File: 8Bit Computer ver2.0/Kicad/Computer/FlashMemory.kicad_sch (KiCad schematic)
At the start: 0 parts

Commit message: Kicad,parts
Kicad:
worked on Flash memory
began RAM
parts:
added Delay Chip for Flash
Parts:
- added IC189: SN74AHC74DR, Samacsys:SOIC127P600X175-14N, symbol Samacsys:SN74AHC74DR
- added IC190, IC192: M29F800FT55N3E2, Samacsys:SOP50P2000X120-48N, symbol Samacsys:M29F800FT55N3E2
- added IC193, IC194, IC195, IC196, IC197, IC198, IC199, IC200, IC201, IC202, IC203, IC204, IC205, IC206: SN74ABT245BDWR, Samacsys:SOIC127P1030X265-20N, symbol Samacsys:SN74ABT245BDWR
- added J1, J2: Conn_02x25_Odd_Even, Connector_PinHeader_2.54mm:PinHeader_2x25_P2.54mm_Vertical, symbol Connector_Generic:Conn_02x25_Odd_Even
- added R1, R10, R2, R3, R4, R5, R6, R7, R8, R9: 4.7k, Resistor_SMD:R_1206_3216Metric_Pad1.30x1.75mm_HandSolder, symbol Device:R
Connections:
- net ADR_{dis}: now also IC189.12 (2D)
- net DAT_{dis}: now also IC189.2 (1D)
- new net: IC204.11 (B8), IC206.9 (A8)
- new net: IC204.12 (B7), IC206.8 (A7)
- new net: IC204.13 (B6), IC206.7 (A6)
- new net: IC204.14 (B5), IC206.6 (A5)
- new net: IC204.15 (B4), IC206.5 (A4)
- new net: IC204.16 (B3), IC206.4 (A3)
- new net: IC204.17 (B2), IC206.3 (A2)
- new net: IC204.18 (B1), IC206.2 (A1)
- new net: IC189.8 (2~{Q}), IC205.19 (~{OE}), IC206.19 (~{OE})
- new net: IC203.18 (B1), IC205.2 (A1)
- new net: IC203.17 (B2), IC205.3 (A2)
- new net: IC203.16 (B3), IC205.4 (A3)
- new net: IC203.15 (B4), IC205.5 (A4)
- new net: IC203.14 (B5), IC205.6 (A5)
- new net: IC203.13 (B6), IC205.7 (A6)
- new net: IC203.12 (B7), IC205.8 (A7)
- new net: IC203.11 (B8), IC205.9 (A8)
- new net: IC189.6 (1~{Q}), IC198.19 (~{OE})
- new net ADR0: IC206.11 (B8)
- new net ADR1: IC206.13 (B6)
- new net ADR10: IC206.16 (B3)
- new net ADR11: IC206.18 (B1)
- new net ADR12: IC205.12 (B7)
- new net ADR13: IC205.14 (B5)
- new net ADR14: IC205.16 (B3)
- new net ADR15: IC205.18 (B1)
- new net ADR2: IC206.15 (B4)
- new net ADR3: IC206.17 (B2)
- new net ADR4: IC205.11 (B8)
- new net ADR5: IC205.13 (B6)
- new net ADR6: IC205.15 (B4)
- new net ADR7: IC205.17 (B2)
- new net ADR8: IC206.12 (B7)
- new net ADR9: IC206.14 (B5)
- new net AMISC0: IC192.11 (WE#), IC197.18 (B1), J1.21 (Pin_21)
- new net AMISC1: IC192.12 (RP#), J1.23 (Pin_23)
- new net AMISC2: IC192.15 (R/B#), J1.29 (Pin_29)
- new net AMISC3: IC192.16 (A18), IC197.15 (B4), J1.31 (Pin_31)
- new net AMISC4: IC192.17 (A17), IC197.14 (B5), J1.33 (Pin_33)
- new net BMISC0: IC192.48 (A16), IC197.13 (B6), J1.2 (Pin_2)
- new net BMISC1: IC192.28 (OE#), IC197.12 (B7), J1.42 (Pin_42)
- new net BMISC2: IC192.26 (CE#), IC197.11 (B8), J1.46 (Pin_46)
- new net CMD0: IC199.11 (B8)
- new net CMD1: IC199.12 (B7)
- new net CMD2: IC199.13 (B6)
- new net CMD3: IC199.14 (B5)
- new net CMD4: IC199.15 (B4)
- new net CMD5: IC199.16 (B3)
- new net CMD6: IC199.17 (B2)
- new net CMD7: IC199.18 (B1)
- new net CMISC0: IC190.11 (WE#), IC202.18 (B1), J2.21 (Pin_21)
- new net CMISC1: IC190.12 (RP#), J2.23 (Pin_23)
- new net CMISC2: IC190.15 (R/B#), J2.29 (Pin_29)
- new net CMISC3: IC190.16 (A18), IC202.15 (B4), J2.31 (Pin_31)
- new net CMISC4: IC190.17 (A17), IC202.14 (B5), J2.33 (Pin_33)
- new net DAT0: IC198.11 (B8)
- new net DAT1: IC198.12 (B7)
- new net DAT2: IC198.13 (B6)
- new net DAT3: IC198.14 (B5)
- new net DAT4: IC198.15 (B4)
- new net DAT5: IC198.16 (B3)
- new net DAT6: IC198.17 (B2)
- new net DAT7: IC198.18 (B1)
- new net DATCMD0: IC192.45 (DQ15A-1), IC195.2 (A1), J1.8 (Pin_8)
- new net DATCMD1: IC192.44 (DQ7), IC195.3 (A2), J1.10 (Pin_10)
- new net DATCMD10: IC192.34 (DQ10), IC196.4 (A3), J1.30 (Pin_30)
- new net DATCMD11: IC192.33 (DQ2), IC196.5 (A4), J1.32 (Pin_32)
- new net DATCMD12: IC192.32 (DQ9), IC196.6 (A5), J1.34 (Pin_34)
- new net DATCMD13: IC192.31 (DQ1), IC196.7 (A6), J1.36 (Pin_36)
- new net DATCMD14: IC192.30 (DQ8), IC196.8 (A7), J1.38 (Pin_38)
- new net DATCMD15: IC192.29 (DQ0), IC196.9 (A8), J1.40 (Pin_40)
- new net DATCMD2: IC192.43 (DQ14), IC195.4 (A3), J1.12 (Pin_12)
- new net DATCMD3: IC192.42 (DQ6), IC195.5 (A4), J1.14 (Pin_14)
- new net DATCMD4: IC192.41 (DQ13), IC195.6 (A5), J1.16 (Pin_16)
- new net DATCMD5: IC192.40 (DQ5), IC195.7 (A6), J1.18 (Pin_18)
- new net DATCMD6: IC192.39 (DQ12), IC195.8 (A7), J1.20 (Pin_20)
- new net DATCMD7: IC192.38 (DQ4), IC195.9 (A8), J1.22 (Pin_22)
- new net DATCMD8: IC192.36 (DQ11), IC196.2 (A1), J1.26 (Pin_26)
- new net DATCMD9: IC192.35 (DQ3), IC196.3 (A2), J1.28 (Pin_28)
- new net DMISC0: IC190.48 (A16), IC202.13 (B6), J2.2 (Pin_2)
- new net DMISC1: IC190.28 (OE#), IC202.12 (B7), J2.42 (Pin_42)
- new net DMISC2: IC190.26 (CE#), IC202.11 (B8), J2.46 (Pin_46)
- new net GND: IC189.7 (GND), IC190.27 (VSS_1), IC190.46 (VSS_2), IC192.27 (VSS_1), IC192.46 (VSS_2), IC193.10 (GND), IC194.10 (GND), IC195.10 (GND), IC196.10 (GND), IC197.10 (GND), IC197.5 (A4), IC197.6 (A5), IC197.7 (A6), IC197.8 (A7), IC197.9 (A8), IC198.10 (GND), IC199.10 (GND), IC199.19 (~{OE}), IC200.10 (GND), IC201.10 (GND), IC202.10 (GND), IC202.5 (A4), IC202.6 (A5), IC202.7 (A6), IC202.8 (A7), IC202.9 (A8), IC203.10 (GND), IC204.10 (GND), IC205.10 (GND), IC206.10 (GND), J1.44 (Pin_44), J1.6 (Pin_6), J2.44 (Pin_44), J2.6 (Pin_6), R1.1, R10.1, R2.1, R3.1, R4.1, R5.1, R6.1, R7.1, R8.1, R9.1
- new net HADR0: IC190.45 (DQ15A-1), IC203.2 (A1), J2.8 (Pin_8)
- new net HADR1: IC190.44 (DQ7), IC203.3 (A2), J2.10 (Pin_10)
- new net HADR10: IC190.34 (DQ10), IC204.4 (A3), J2.30 (Pin_30)
- new net HADR11: IC190.33 (DQ2), IC204.5 (A4), J2.32 (Pin_32)
- new net HADR12: IC190.32 (DQ9), IC204.6 (A5), J2.34 (Pin_34)
- new net HADR13: IC190.31 (DQ1), IC204.7 (A6), J2.36 (Pin_36)
- new net HADR14: IC190.30 (DQ8), IC204.8 (A7), J2.38 (Pin_38)
- new net HADR15: IC190.29 (DQ0), IC204.9 (A8), J2.40 (Pin_40)
- new net HADR2: IC190.43 (DQ14), IC203.4 (A3), J2.12 (Pin_12)
- new net HADR3: IC190.42 (DQ6), IC203.5 (A4), J2.14 (Pin_14)
- new net HADR4: IC190.41 (DQ13), IC203.6 (A5), J2.16 (Pin_16)
- new net HADR5: IC190.40 (DQ5), IC203.7 (A6), J2.18 (Pin_18)
- new net HADR6: IC190.39 (DQ12), IC203.8 (A7), J2.20 (Pin_20)
- new net HADR7: IC190.38 (DQ4), IC203.9 (A8), J2.22 (Pin_22)
- new net HADR8: IC190.36 (DQ11), IC204.2 (A1), J2.26 (Pin_26)
- new net HADR9: IC190.35 (DQ3), IC204.3 (A2), J2.28 (Pin_28)
- new net HDATCMD0: IC195.18 (B1), IC198.2 (A1)
- new net HDATCMD1: IC195.17 (B2), IC199.2 (A1)
- new net HDATCMD10: IC196.16 (B3), IC198.7 (A6)
- new net HDATCMD11: IC196.15 (B4), IC199.7 (A6)
- new net HDATCMD12: IC196.14 (B5), IC198.8 (A7)
- new net HDATCMD13: IC196.13 (B6), IC199.8 (A7)
- new net HDATCMD14: IC196.12 (B7), IC198.9 (A8)
- new net HDATCMD15: IC196.11 (B8), IC199.9 (A8)
- new net HDATCMD2: IC195.16 (B3), IC198.3 (A2)
- new net HDATCMD3: IC195.15 (B4), IC199.3 (A2)
- new net HDATCMD4: IC195.14 (B5), IC198.4 (A3)
- new net HDATCMD5: IC195.13 (B6), IC199.4 (A3)
- new net HDATCMD6: IC195.12 (B7), IC198.5 (A4)
- new net HDATCMD7: IC195.11 (B8), IC199.5 (A4)
- new net HDATCMD8: IC196.18 (B1), IC198.6 (A5)
- new net HDATCMD9: IC196.17 (B2), IC199.6 (A5)
- new net LN0: IC194.9 (A8), IC201.9 (A8)
- new net LN1: IC194.8 (A7), IC201.8 (A7)
- new net LN10: IC193.7 (A6), IC200.7 (A6)
- new net LN11: IC193.6 (A5), IC200.6 (A5)
- new net LN12: IC193.5 (A4), IC200.5 (A4)
- new net LN13: IC193.4 (A3), IC200.4 (A3)
- new net LN14: IC193.3 (A2), IC200.3 (A2)
- new net LN15: IC193.2 (A1), IC200.2 (A1)
- new net LN2: IC194.7 (A6), IC201.7 (A6)
- new net LN3: IC194.6 (A5), IC201.6 (A5)
- new net LN4: IC194.5 (A4), IC201.5 (A4)
- new net LN5: IC194.4 (A3), IC201.4 (A3)
- new net LN6: IC194.3 (A2), IC201.3 (A2)
- new net LN7: IC194.2 (A1), IC201.2 (A1)
- new net LN8: IC193.9 (A8), IC200.9 (A8)
- new net LN9: IC193.8 (A7), IC200.8 (A7)
- new net LNHADR0: IC190.1 (A15), IC200.18 (B1), J2.1 (Pin_1)
- new net LNHADR1: IC190.2 (A14), IC200.17 (B2), J2.3 (Pin_3)
- new net LNHADR10: IC190.20 (A5), IC201.16 (B3), J2.39 (Pin_39)
- new net LNHADR11: IC190.21 (A4), IC201.15 (B4), J2.41 (Pin_41)
- new net LNHADR12: IC190.22 (A3), IC201.14 (B5), J2.43 (Pin_43)
- new net LNHADR13: IC190.23 (A2), IC201.13 (B6), J2.45 (Pin_45)
- new net LNHADR14: IC190.24 (A1), IC201.12 (B7), J2.47 (Pin_47)
- new net LNHADR15: IC190.25 (A0), IC201.11 (B8), J2.48 (Pin_48)
- new net LNHADR2: IC190.3 (A13), IC200.16 (B3), J2.5 (Pin_5)
- new net LNHADR3: IC190.4 (A12), IC200.15 (B4), J2.7 (Pin_7)
- new net LNHADR4: IC190.5 (A11), IC200.14 (B5), J2.9 (Pin_9)
- new net LNHADR5: IC190.6 (A10), IC200.13 (B6), J2.11 (Pin_11)
- new net LNHADR6: IC190.7 (A9), IC200.12 (B7), J2.13 (Pin_13)
- new net LNHADR7: IC190.8 (A8), IC200.11 (B8), J2.15 (Pin_15)
- new net LNHADR8: IC190.18 (A7), IC201.18 (B1), J2.35 (Pin_35)
- new net LNHADR9: IC190.19 (A6), IC201.17 (B2), J2.37 (Pin_37)
- new net LNHCD0: IC192.1 (A15), IC193.18 (B1), J1.1 (Pin_1)
- new net LNHCD1: IC192.2 (A14), IC193.17 (B2), J1.3 (Pin_3)
- new net LNHCD10: IC192.20 (A5), IC194.16 (B3), J1.39 (Pin_39)
- new net LNHCD11: IC192.21 (A4), IC194.15 (B4), J1.41 (Pin_41)
- new net LNHCD12: IC192.22 (A3), IC194.14 (B5), J1.43 (Pin_43)
- new net LNHCD13: IC192.23 (A2), IC194.13 (B6), J1.45 (Pin_45)
- new net LNHCD14: IC192.24 (A1), IC194.12 (B7), J1.47 (Pin_47)
- new net LNHCD15: IC192.25 (A0), IC194.11 (B8), J1.48 (Pin_48)
- new net LNHCD2: IC192.3 (A13), IC193.16 (B3), J1.5 (Pin_5)
- new net LNHCD3: IC192.4 (A12), IC193.15 (B4), J1.7 (Pin_7)
- new net LNHCD4: IC192.5 (A11), IC193.14 (B5), J1.9 (Pin_9)
- new net LNHCD5: IC192.6 (A10), IC193.13 (B6), J1.11 (Pin_11)
- new net LNHCD6: IC192.7 (A9), IC193.12 (B7), J1.13 (Pin_13)
- new net LNHCD7: IC192.8 (A8), IC193.11 (B8), J1.15 (Pin_15)
- new net LNHCD8: IC192.18 (A7), IC194.18 (B1), J1.35 (Pin_35)
- new net LNHCD9: IC192.19 (A6), IC194.17 (B2), J1.37 (Pin_37)
- new net ProgModeADR: IC200.19 (~{OE}), IC201.19 (~{OE}), IC202.19 (~{OE}), IC203.19 (~{OE}), IC204.19 (~{OE}), J2.50 (Pin_50), R10.2, R6.2, R7.2, R8.2, R9.2
- new net ProgModeCD: IC193.19 (~{OE}), IC194.19 (~{OE}), IC195.19 (~{OE}), IC196.19 (~{OE}), IC197.19 (~{OE}), J1.50 (Pin_50), R1.2, R2.2, R3.2, R4.2, R5.2
- new net VCC: IC189.1 (1~{CLR}), IC189.10 (2~{PRE}), IC189.13 (2~{CLR}), IC189.14 (VCC), IC189.4 (1~{PRE}), IC190.37 (VCC), IC190.47 (BYTE#), IC192.37 (VCC), IC192.47 (BYTE#), IC193.1 (DIR), IC193.20 (VCC), IC194.1 (DIR), IC194.20 (VCC), IC195.1 (DIR), IC195.20 (VCC), IC196.1 (DIR), IC196.20 (VCC), IC197.1 (DIR), IC197.2 (A1), IC197.20 (VCC), IC198.1 (DIR), IC198.20 (VCC), IC199.1 (DIR), IC199.20 (VCC), IC200.1 (DIR), IC200.20 (VCC), IC201.1 (DIR), IC201.20 (VCC), IC202.1 (DIR), IC202.2 (A1), IC202.20 (VCC), IC203.1 (DIR), IC203.20 (VCC), IC204.1 (DIR), IC204.20 (VCC), IC205.1 (DIR), IC205.20 (VCC), IC206.1 (DIR), IC206.20 (VCC), J1.49 (Pin_49), J2.49 (Pin_49)
- no-connect marks 0 -> 28
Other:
- note added: "ADR Flash Programport"
- note added: "Connect ProgModeADR to VCC via the cable adapter on the programmer side"
- note added: "Connect ProgModeCD to VCC via the cable adapter on the programmer side"
- note added: "DATA and CMD Flash Programport"

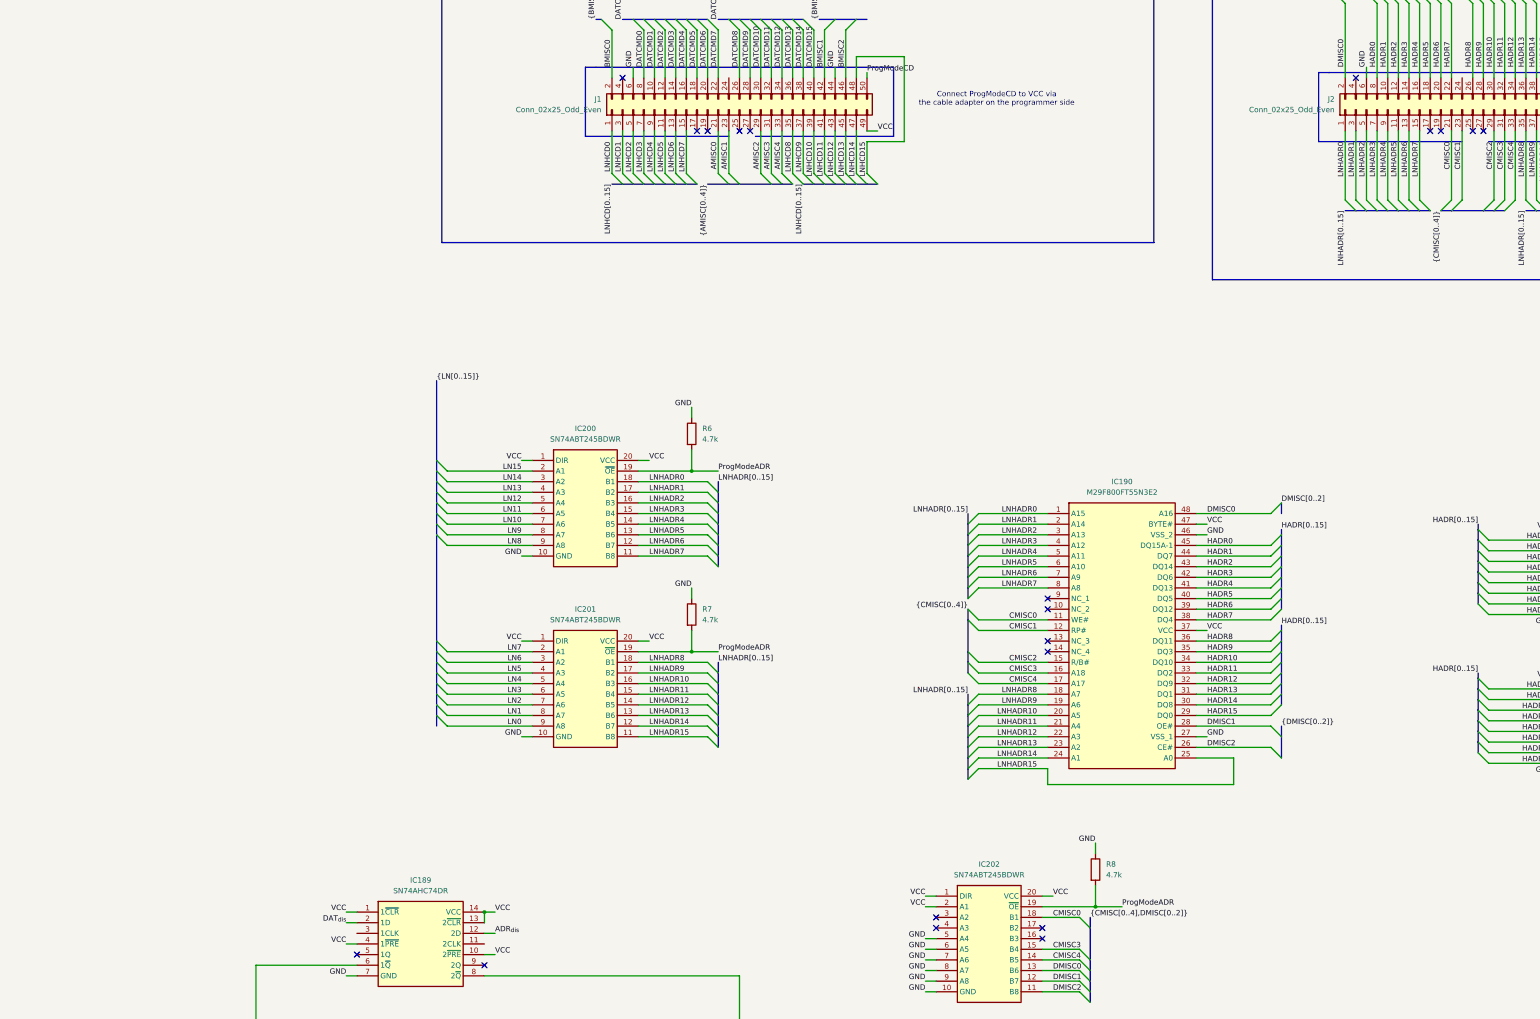
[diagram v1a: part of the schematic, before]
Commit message: Kicad
included Delay, pin Strips and headers, 8xnot
added some comps
finished flash mem
added DATtoADR
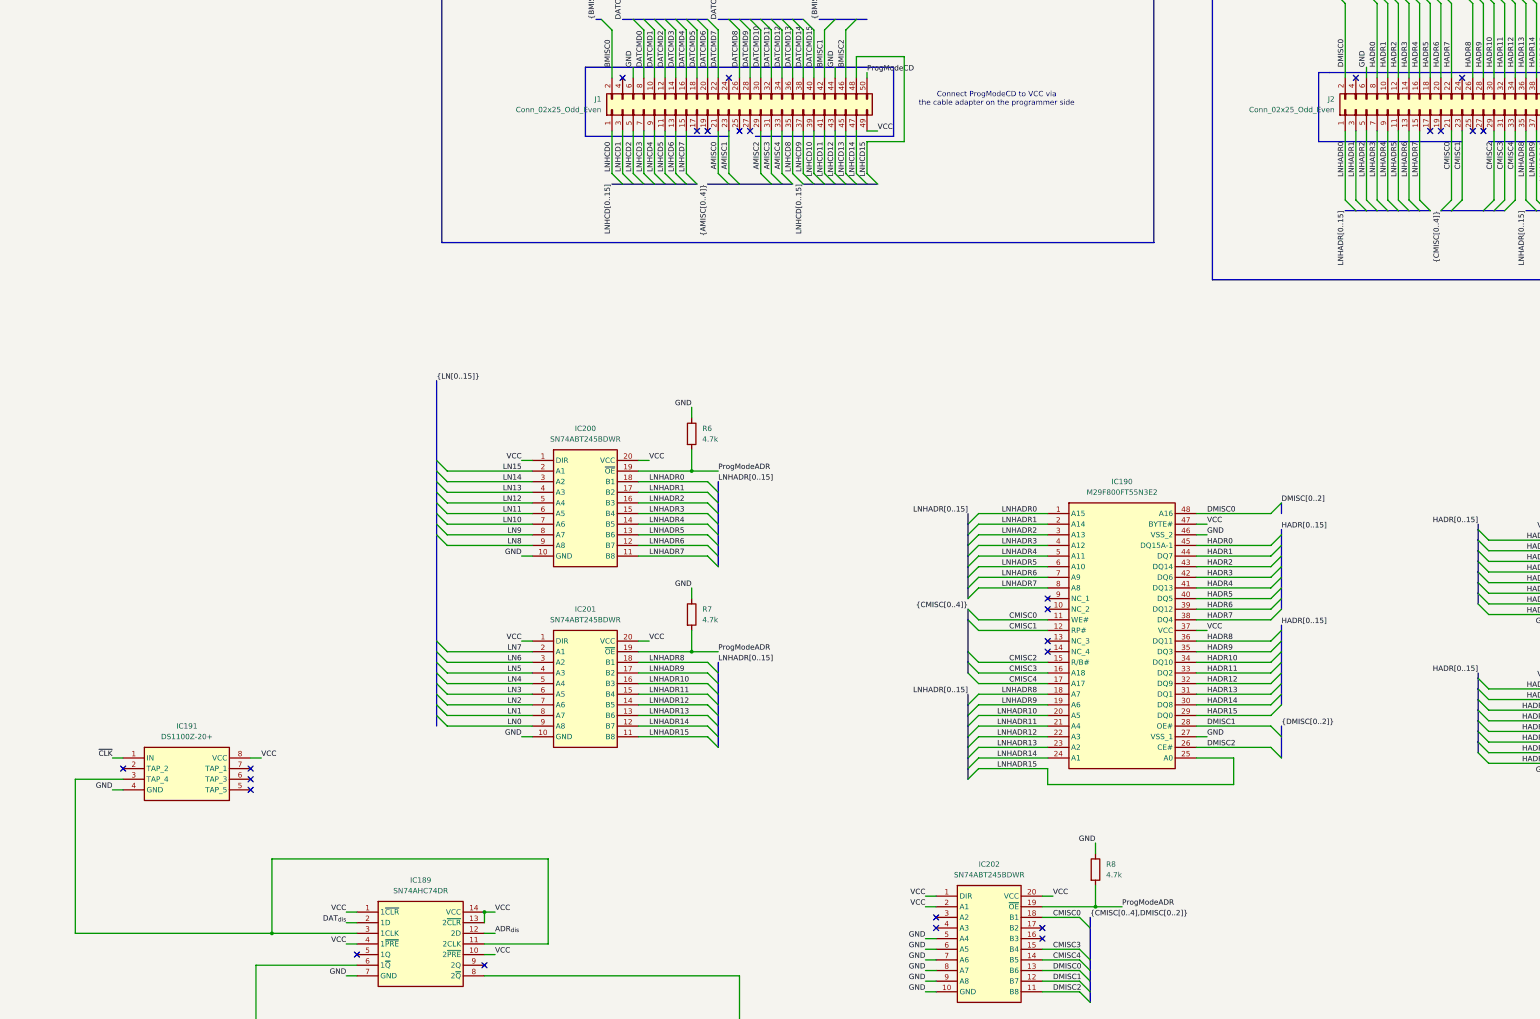
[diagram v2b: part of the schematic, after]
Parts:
- added IC191: DS1100Z-20+, Samacsys:SOIC127P600X175-8N, symbol Samacsys:DS1100Z-20+
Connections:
- net GND: now also IC191.4 (GND)
- net VCC: now also IC191.8 (VCC)
- net ~{CLK}: now also IC191.1 (IN)
- net at IC189.11 (2CLK): now also IC189.3 (1CLK), IC191.3 (TAP_4)
- no-connect marks 28 -> 34

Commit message: Kicad
changed to module version
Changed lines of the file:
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@@
 		)
 	)
-	(label "{ADR[0..15]}"
+	(label "ADR[0..15]"
 		(at 603.25 212.09 0)
 		(effects
@@
 		)
 	)
-	(label "{LN[0..15]}"
+	(label "LN[0..15]"
 		(at 189.23 332.74 0)
 		(effects
@@
 		)
 	)
-	(label "{LN[0..15]}"
+	(label "LN[0..15]"
 		(at 73.66 162.56 0)
 		(effects
@@
 		)
 	)
-	(label "{ADR[0..15]}"
+	(label "ADR[0..15]"
 		(at 73.66 149.86 0)
 		(effects
@@
 		)
 	)
-	(label "{LN[0..15]}"
+	(label "LN[0..15]"
 		(at 223.52 172.72 0)
 		(effects
@@
 		)
 	)
-	(hierarchical_label "{LN[0..15]}"
+	(hierarchical_label "LN[0..15]"
 		(shape tri_state)
 		(at 69.85 162.56 180)
@@
 		)
 	)
-	(hierarchical_label "{ADR[0..15]}"
+	(hierarchical_label "ADR[0..15]"
 		(shape tri_state)
 		(at 69.85 149.86 180)
